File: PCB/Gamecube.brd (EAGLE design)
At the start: 58.5 x 61 mm, 13 parts

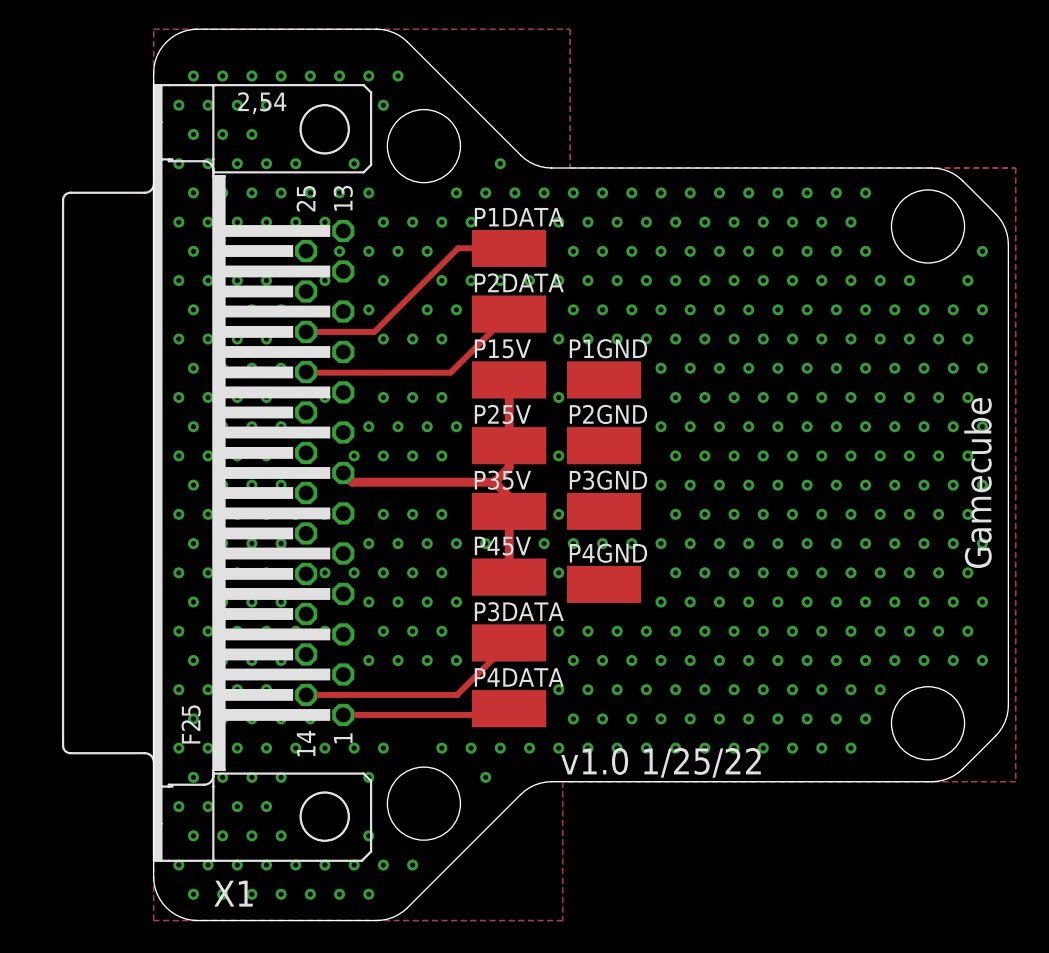
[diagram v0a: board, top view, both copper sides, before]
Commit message: PCB Update for better Housing Fit
All the PCBs were updated for better housing fitment.

Common Changes across all PCBs:
1. All Aux PCBs are now the exact same size.  (there was a .1mm-.5mm Variance previous)
2. All Aux PCBs Mounting holes are in the same location (there was a .05mm-.1mm Variance previous)
3. The DB25 has been moved 1.2mm close to the edge of the PCB for better connection when in the housing.

PCB Specific Updates:
3DO - Rename Pads (Removed trailing numbers), Flipped U2 to match U1, Moved U1 & U2 to same coordinates as other 2 Component PCBs in collection.

PCE & NES- Moved U1 & U2 to same coordinates as other 2 Component PCBs in collection.

PS2/PSX & Saturn - Added Notch on back edge of PCB for access for wires that need to attach to bottom layer of PCB.

All Gerbers have been updated.

New PCBs have been ordered for testing.
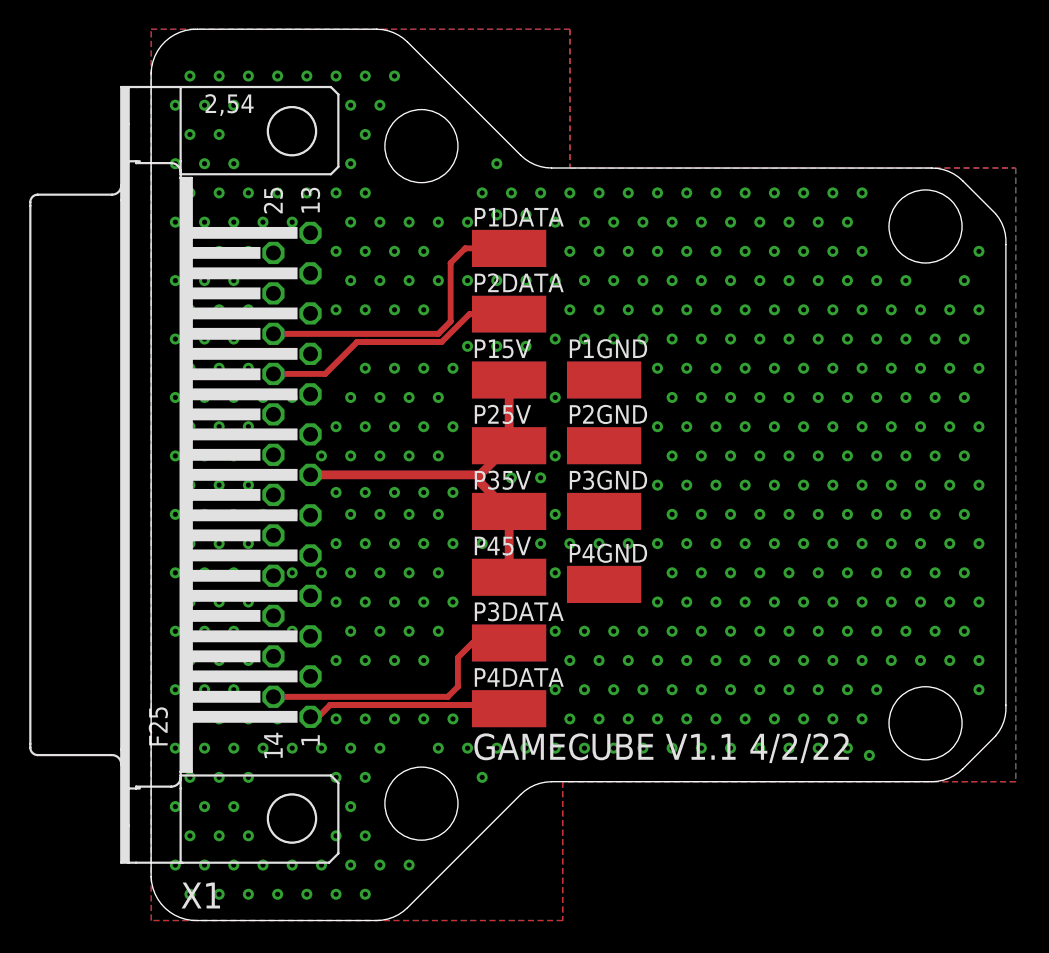
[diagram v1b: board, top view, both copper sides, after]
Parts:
- moved X1 2.24 mm to (9.64, 30.5)
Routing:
- net IO19: track 16.3 -> 20.9 mm
- net IO26: track 15.4 -> 18.8 mm
- net IO27: track 11.5 -> 14.2 mm
- net IO5: track 15.6 -> 17.8 mm
- net 5VIN: track 24.9 -> 26.7 mm
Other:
- outline, holes or cut-outs redrawn
- board text added: "GAMECUBE V1.1 4/2/22"
- board text removed: "Gamecube"
- board text removed: "v1.0 1/25/22"

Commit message: Changed Player Order for N64 and Gamecube
Reversed the player order of the pads on the PCB, when installing in the housing the controller wires would twist.  this resolves that issue.
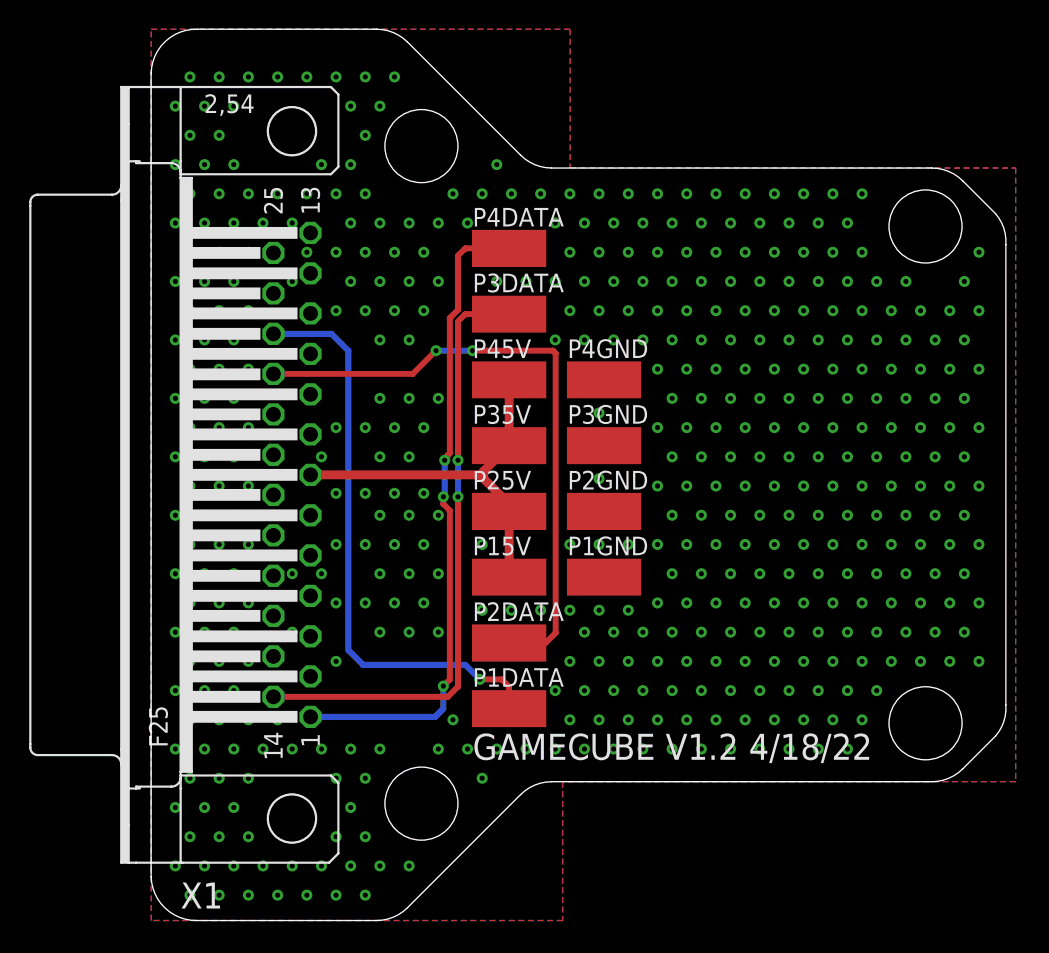
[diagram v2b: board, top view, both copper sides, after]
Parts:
- moved P1DATA 31.5 mm to (24.5, 14.5)
- moved P4DATA 31.5 mm to (24.5, 46.0)
- moved P2DATA 22.5 mm to (24.5, 19.0)
- moved P3DATA 22.5 mm to (24.5, 41.5)
- moved P4GND 14.0 mm to (31.0, 37.0)
- moved P15V 13.5 mm to (24.5, 23.5)
- moved P1GND 13.5 mm to (31.0, 23.5)
- moved P45V 13.5 mm to (24.5, 37.0)
- moved P25V 4.50 mm to (24.5, 28.0)
- moved P2GND 4.50 mm to (31.0, 28.0)
- moved P35V 4.50 mm to (24.5, 32.5)
- moved P3GND 4.50 mm to (31.0, 32.5)
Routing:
- net IO27: track 14.2 -> 44.8 mm, vias 0 -> 3
- net IO5: track 17.8 -> 42.7 mm, vias 0 -> 2
- net IO26: track 18.8 -> 41.6 mm, vias 0 -> 2
- net IO19: track 20.9 -> 39.6 mm, vias 0 -> 1
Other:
- board text added: "GAMECUBE V1.2 4/18/22"
- board text removed: "GAMECUBE V1.1 4/2/22"

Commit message: Added exposed GND plane at DB25 anchors
All PCBs have been update to have exposed GND plane pads for the DB25 anchor points.

This resolves Issue 54
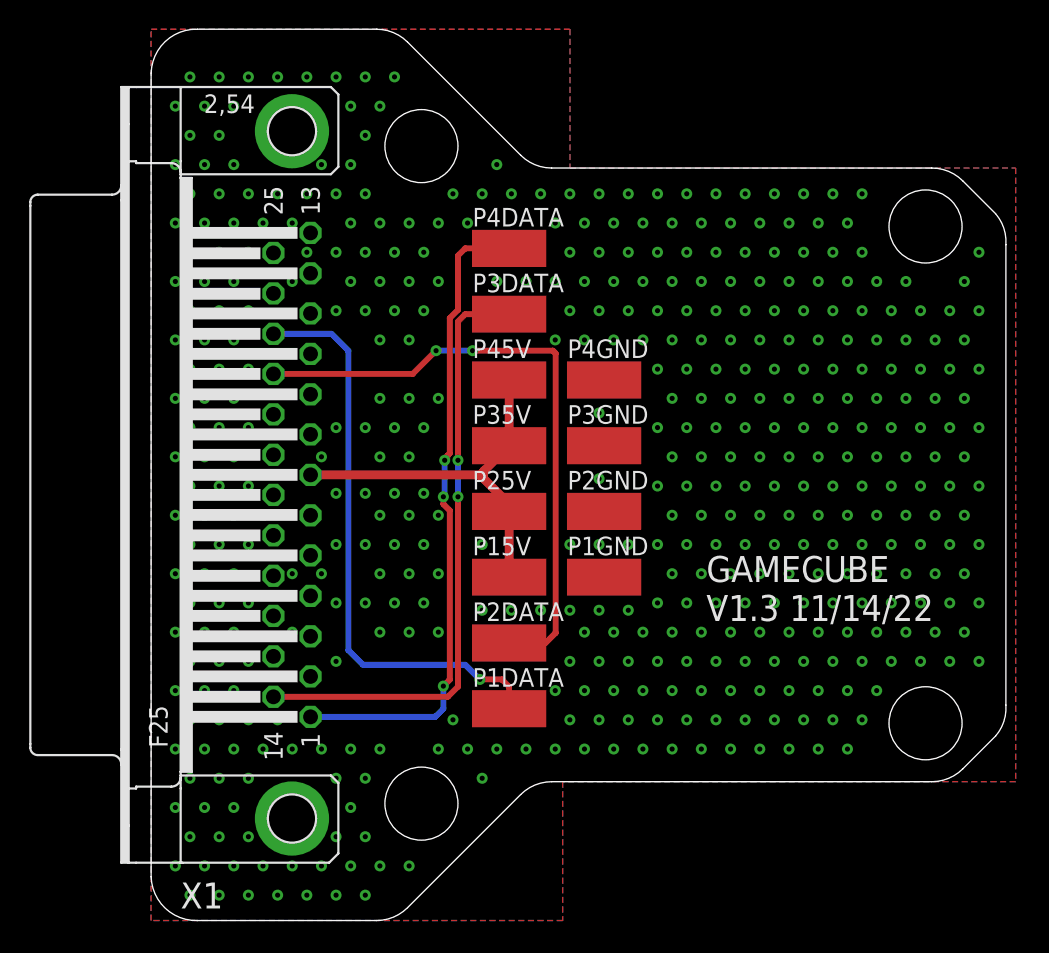
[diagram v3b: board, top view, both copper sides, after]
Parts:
- X1: device SparkFun-Retired:F25H -> SparkFun-Retired:F25HP
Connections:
- net GND: now also X1.GND1, X1.GND2
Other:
- board text added: "GAMECUBE V1.3 11/14/22"
- board text removed: "GAMECUBE V1.2 4/18/22"
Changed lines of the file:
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@@
 <hole x="18.5" y="53" drill="5"/>
 <hole x="18.5" y="8" drill="5"/>
-<text x="22" y="11" size="1.778" layer="21">GAMECUBE V1.2 4/18/22</text>
+<text x="38" y="20.5" size="1.778" layer="21">GAMECUBE
+V1.3 11/14/22</text>
 </plain>
 <attributes>
@@
 <attribute name="VALUE" x="31" y="37" size="0.0254" layer="27" rot="R270"/>
 </element>
-<element name="X1" library="SparkFun-Retired" package="F25H" value="" x="9.64" y="30.5" smashed="yes" rot="R90">
+<element name="X1" library="SparkFun-Retired" package="F25HP" value="" x="9.64" y="30.5" smashed="yes" rot="R90">
 <attribute name="NAME" x="4.919" y="2.6" size="1.778" layer="25" ratio="10" rot="R180"/>
 <attribute name="VALUE" x="-4.33" y="22.118" size="1.778" layer="27" ratio="10" rot="R90"/>
@@
 <via x="55.6568" y="43.735840625" extent="1-16" drill="0.35"/>
 <via x="56.6568" y="45.735840625" extent="1-16" drill="0.35"/>
+<contactref element="X1" pad="GND1"/>
+<contactref element="X1" pad="GND2"/>
 </signal>
 <signal name="5VIN">
@@
 </drawing>
 <compatibility>
+<note version="6.3" minversion="6.2.2" severity="warning">
+Since Version 6.2.2 text objects can contain more than one line,
+which will not be processed correctly with this version.
+</note>
 <note version="8.2" severity="warning">
 Since Version 8.2, EAGLE supports online libraries. The ids
